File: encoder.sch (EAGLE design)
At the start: 3 parts

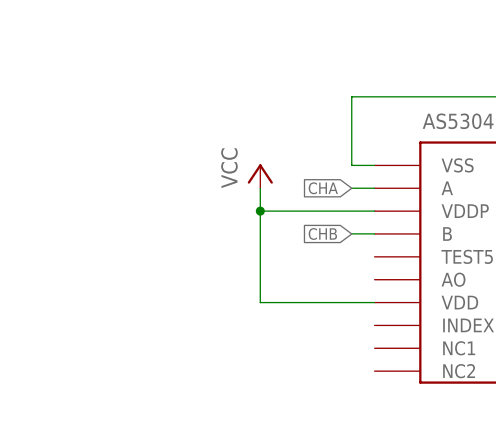
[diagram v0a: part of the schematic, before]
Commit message: pcb do enkoderow i poprawione lbr
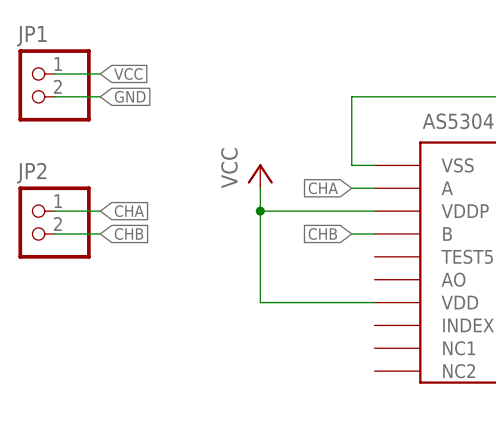
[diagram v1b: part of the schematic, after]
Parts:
- added JP1, JP2: PINHD_1X2_ROUND, _microMouse:PINHD_1X2_ROUND
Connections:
- net CHA: now also JP2.1
- net CHB: now also JP2.2
- net GND: now also JP1.2
- net VCC: now also JP1.1
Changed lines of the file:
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@@
 <part name="C1" library="rcl" deviceset="C-EU" device="C0603" value="10u"/>
 <part name="C2" library="rcl" deviceset="C-EU" device="C0603" value="100n"/>
+<part name="JP1" library="_microMouse" deviceset="PINHD_1X2_ROUND" device=""/>
+<part name="JP2" library="_microMouse" deviceset="PINHD_1X2_ROUND" device=""/>
 </parts>
 <sheets>
@@
 <attribute name="VALUE" x="29.464" y="-9.779" size="1.778" layer="96"/>
 </instance>
+<instance part="JP1" gate="G$1" x="-53.34" y="19.05"/>
+<instance part="JP2" gate="G$1" x="-53.34" y="3.81"/>
 </instances>
 <busses>
@@
 <junction x="27.94" y="-12.7"/>
 </segment>
+<segment>
+<wire x1="-53.34" y1="17.78" x2="-48.26" y2="17.78" width="0.1524" layer="91"/>
+<label x="-48.26" y="17.78" size="1.27" layer="95" xref="yes"/>
+<pinref part="JP1" gate="G$1" pin="2"/>
+</segment>
 </net>
 <net name="CHA" class="0">
@@
 <label x="-20.32" y="7.62" size="1.27" layer="95" rot="R180" xref="yes"/>
 </segment>
+<segment>
+<wire x1="-53.34" y1="5.08" x2="-48.26" y2="5.08" width="0.1524" layer="91"/>
+<label x="-48.26" y="5.08" size="1.27" layer="95" xref="yes"/>
+<pinref part="JP2" gate="G$1" pin="1"/>
+</segment>
 </net>
 <net name="CHB" class="0">
@@
 <wire x1="-17.78" y1="2.54" x2="-20.32" y2="2.54" width="0.1524" layer="91"/>
 <label x="-20.32" y="2.54" size="1.27" layer="95" rot="R180" xref="yes"/>
+</segment>
+<segment>
+<wire x1="-53.34" y1="2.54" x2="-48.26" y2="2.54" width="0.1524" layer="91"/>
+<label x="-48.26" y="2.54" size="1.27" layer="95" xref="yes"/>
+<pinref part="JP2" gate="G$1" pin="2"/>
 </segment>
 </net>
@@
 <junction x="27.94" y="0"/>
 </segment>
+<segment>
+<wire x1="-53.34" y1="20.32" x2="-48.26" y2="20.32" width="0.1524" layer="91"/>
+<label x="-48.26" y="20.32" size="1.27" layer="95" xref="yes"/>
+<pinref part="JP1" gate="G$1" pin="1"/>
+</segment>
 </net>

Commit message: poprawa bledow, dodanie rezystorow na wyjsciach stm-glownie w modolach, poprawa elementu 9axis z biblioteki
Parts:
- added JP3, JP8: (no value), pinhead:PINHD-1X1
- added JP4, JP5, JP6, JP7: PINHD_1X2_ROUND, _microMouse:PINHD_1X2_ROUND
- added R1, R2: (no value), rcl:R-EU_R0805
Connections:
- new net AO: IC1.AO, JP3.1
- new net N$1: JP2.1, R1.1
- new net N$2: JP2.2, R2.2
- net CHA: now also R1.2; no longer JP2.1
- net CHB: now also R2.1; no longer JP2.2
- net GND: now also JP4.2, JP8.1
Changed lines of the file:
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@@
 <part name="JP1" library="_microMouse" deviceset="PINHD_1X2_ROUND" device=""/>
 <part name="JP2" library="_microMouse" deviceset="PINHD_1X2_ROUND" device=""/>
+<part name="R1" library="rcl" deviceset="R-EU_" device="R0805"/>
+<part name="R2" library="rcl" deviceset="R-EU_" device="R0805"/>
+<part name="JP3" library="pinhead" deviceset="PINHD-1X1" device=""/>
+<part name="JP4" library="_microMouse" deviceset="PINHD_1X2_ROUND" device=""/>
+<part name="JP5" library="_microMouse" deviceset="PINHD_1X2_ROUND" device=""/>
+<part name="JP6" library="_microMouse" deviceset="PINHD_1X2_ROUND" device=""/>
+<part name="JP7" library="_microMouse" deviceset="PINHD_1X2_ROUND" device=""/>
+<part name="JP8" library="pinhead" deviceset="PINHD-1X1" device=""/>
+<part name="GND3" library="supply1" deviceset="GND" device=""/>
+<part name="GND4" library="supply1" deviceset="GND" device=""/>
 </parts>
 <sheets>
@@
 <instance part="JP1" gate="G$1" x="-53.34" y="19.05"/>
 <instance part="JP2" gate="G$1" x="-53.34" y="3.81"/>
+<instance part="R1" gate="G$1" x="-48.26" y="5.08"/>
+<instance part="R2" gate="G$1" x="-48.26" y="2.54" rot="R180"/>
+<instance part="JP3" gate="G$1" x="-55.88" y="-7.62" rot="R180"/>
+<instance part="JP4" gate="G$1" x="-60.96" y="19.05"/>
+<instance part="JP5" gate="G$1" x="-60.96" y="3.81"/>
+<instance part="JP6" gate="G$1" x="-68.58" y="3.81"/>
+<instance part="JP7" gate="G$1" x="-68.58" y="19.05"/>
+<instance part="JP8" gate="G$1" x="-55.88" y="-12.7" rot="R180"/>
+<instance part="GND3" gate="1" x="-45.72" y="-12.7" rot="R90"/>
+<instance part="GND4" gate="1" x="-60.96" y="15.24"/>
 </instances>
 <busses>
@@
 <pinref part="JP1" gate="G$1" pin="2"/>
 </segment>
+<segment>
+<pinref part="JP8" gate="G$1" pin="1"/>
+<pinref part="GND3" gate="1" pin="GND"/>
+<wire x1="-53.34" y1="-12.7" x2="-48.26" y2="-12.7" width="0.1524" layer="91"/>
+</segment>
+<segment>
+<pinref part="JP4" gate="G$1" pin="2"/>
+<pinref part="GND4" gate="1" pin="GND"/>
+</segment>
 </net>
 <net name="CHA" class="0">
@@
 </segment>
 <segment>
-<wire x1="-53.34" y1="5.08" x2="-48.26" y2="5.08" width="0.1524" layer="91"/>
-<label x="-48.26" y="5.08" size="1.27" layer="95" xref="yes"/>
-<pinref part="JP2" gate="G$1" pin="1"/>
+<pinref part="R1" gate="G$1" pin="2"/>
+<wire x1="-43.18" y1="5.08" x2="-40.64" y2="5.08" width="0.1524" layer="91"/>
+<label x="-40.64" y="5.08" size="1.27" layer="95" xref="yes"/>
 </segment>
 </net>
@@
 </segment>
 <segment>
-<wire x1="-53.34" y1="2.54" x2="-48.26" y2="2.54" width="0.1524" layer="91"/>
-<label x="-48.26" y="2.54" size="1.27" layer="95" xref="yes"/>
-<pinref part="JP2" gate="G$1" pin="2"/>
+<pinref part="R2" gate="G$1" pin="1"/>
+<wire x1="-43.18" y1="2.54" x2="-40.64" y2="2.54" width="0.1524" layer="91"/>
+<label x="-40.64" y="2.54" size="1.27" layer="95" xref="yes"/>
 </segment>
 </net>
@@
 </segment>
 </net>
+<net name="N$1" class="0">
+<segment>
+<pinref part="JP2" gate="G$1" pin="1"/>
+<pinref part="R1" gate="G$1" pin="1"/>
+</segment>
+</net>
+<net name="N$2" class="0">
+<segment>
+<pinref part="JP2" gate="G$1" pin="2"/>
+<pinref part="R2" gate="G$1" pin="2"/>
+</segment>
+</net>
+<net name="AO" class="0">
+<segment>
+<pinref part="IC1" gate="G$1" pin="AO"/>
+<wire x1="-17.78" y1="-2.54" x2="-20.32" y2="-2.54" width="0.1524" layer="91"/>
+<label x="-20.32" y="-2.54" size="1.27" layer="95" rot="R180" xref="yes"/>
+</segment>
+<segment>
+<pinref part="JP3" gate="G$1" pin="1"/>
+<wire x1="-53.34" y1="-7.62" x2="-45.72" y2="-7.62" width="0.1524" layer="91"/>
+<label x="-45.72" y="-7.62" size="1.27" layer="95" xref="yes"/>
+</segment>
+</net>

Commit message: gerbery
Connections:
- net GND: now also JP7.2
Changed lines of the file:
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@@
 <part name="JP4" library="_microMouse" deviceset="PINHD_1X2_ROUND" device=""/>
 <part name="JP5" library="_microMouse" deviceset="PINHD_1X2_ROUND" device=""/>
-<part name="JP6" library="_microMouse" deviceset="PINHD_1X2_ROUND" device=""/>
-<part name="JP7" library="_microMouse" deviceset="PINHD_1X2_ROUND" device=""/>
 <part name="JP8" library="pinhead" deviceset="PINHD-1X1" device=""/>
 <part name="GND3" library="supply1" deviceset="GND" device=""/>
 <part name="GND4" library="supply1" deviceset="GND" device=""/>
+<part name="JP6" library="_microMouse" deviceset="PINHD_1X2_ROUND" device=""/>
+<part name="JP7" library="_microMouse" deviceset="PINHD_1X2_ROUND" device=""/>
+<part name="GND5" library="supply1" deviceset="GND" device=""/>
 </parts>
 <sheets>
@@
 <instance part="JP4" gate="G$1" x="-60.96" y="19.05"/>
 <instance part="JP5" gate="G$1" x="-60.96" y="3.81"/>
-<instance part="JP6" gate="G$1" x="-68.58" y="3.81"/>
-<instance part="JP7" gate="G$1" x="-68.58" y="19.05"/>
 <instance part="JP8" gate="G$1" x="-55.88" y="-12.7" rot="R180"/>
 <instance part="GND3" gate="1" x="-45.72" y="-12.7" rot="R90"/>
 <instance part="GND4" gate="1" x="-60.96" y="15.24"/>
+<instance part="JP6" gate="G$1" x="-68.58" y="3.81"/>
+<instance part="JP7" gate="G$1" x="-68.58" y="19.05"/>
+<instance part="GND5" gate="1" x="-68.58" y="15.24"/>
 </instances>
 <busses>
@@
 <pinref part="GND4" gate="1" pin="GND"/>
 </segment>
+<segment>
+<pinref part="JP7" gate="G$1" pin="2"/>
+<pinref part="GND5" gate="1" pin="GND"/>
+</segment>
 </net>
